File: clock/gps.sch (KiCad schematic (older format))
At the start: 16 parts, among them P301 MCRF, Q301 BSS138, Q302 BSS138, U301 Adafruit746, U302 MIC5225, U303 PA6H

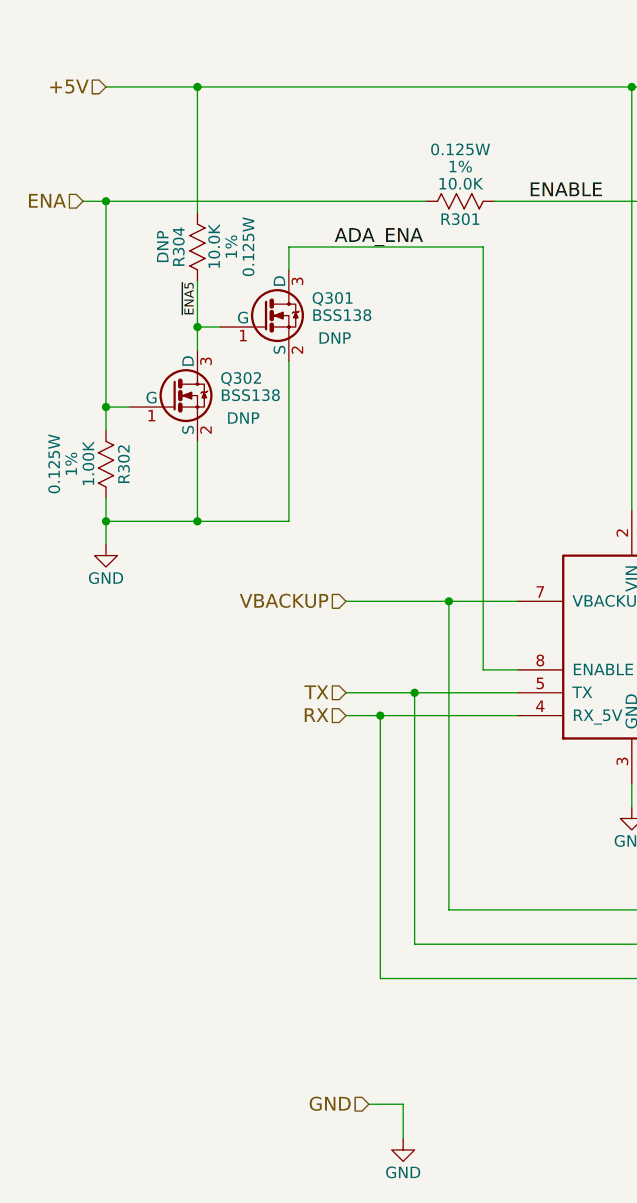
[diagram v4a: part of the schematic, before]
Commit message: Remove sheet to sheet power interconnect because power symbols are global.
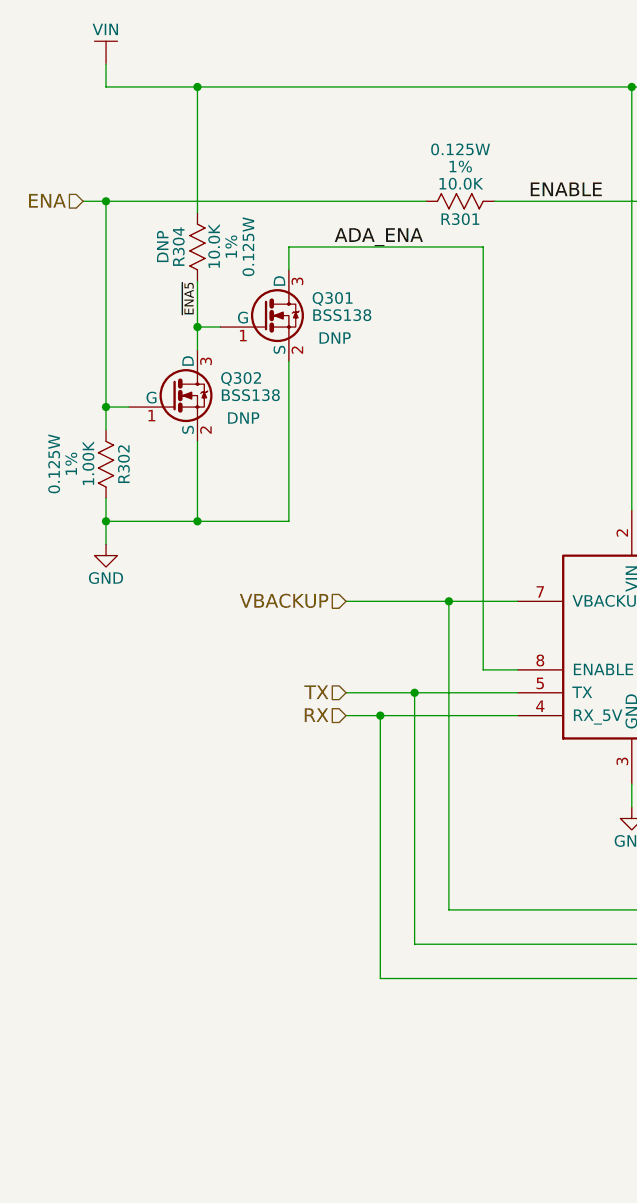
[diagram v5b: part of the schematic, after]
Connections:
- net +5V renamed VIN
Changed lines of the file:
@@
 $EndComp
 $Comp
-L GND #PWR305
+L GND #PWR042
 U 1 1 56235A8F
 P 7200 5350
-F 0 "#PWR305" H 7200 5100 50  0001 C CNN
+F 0 "#PWR042" H 7200 5100 50  0001 C CNN
 F 1 "GND" H 7200 5200 50  0000 C CNN
 F 2 "" H 7200 5350 60  0000 C CNN
@@
 Connection ~ 7100 1900
 $Comp
-L GND #PWR306
+L GND #PWR043
 U 1 1 56235D57
 P 8000 2650
-F 0 "#PWR306" H 8000 2400 50  0001 C CNN
+F 0 "#PWR043" H 8000 2400 50  0001 C CNN
 F 1 "GND" H 8000 2500 50  0000 C CNN
 F 2 "" H 8000 2650 60  0000 C CNN
@@
 Connection ~ 5250 2550
 Connection ~ 7100 2550
-Text HLabel 1450 1600 0    60   Input ~ 0
-+5V
 Text HLabel 1350 2100 0    60   Input ~ 0
 ENA
@@
 	5200 3650 6300 3650
 $Comp
-L GND #PWR304
+L GND #PWR044
 U 1 1 56236310
 P 4950 3350
-F 0 "#PWR304" H 4950 3100 50  0001 C CNN
+F 0 "#PWR044" H 4950 3100 50  0001 C CNN
 F 1 "GND" H 4950 3200 50  0000 C CNN
 F 2 "" H 4950 3350 60  0000 C CNN
@@
 	2500 3850 3250 3850
 $Comp
-L GND #PWR303
+L GND #PWR045
 U 1 1 56236487
 P 3750 4750
-F 0 "#PWR303" H 3750 4500 50  0001 C CNN
+F 0 "#PWR045" H 3750 4500 50  0001 C CNN
 F 1 "GND" H 3750 4600 50  0000 C CNN
 F 2 "" H 3750 4750 60  0000 C CNN
@@
 Wire Wire Line
 	7100 2300 7100 2550
-Text HLabel 2600 6050 0    60   Input ~ 0
-GND
-$Comp
-L GND #PWR302
-U 1 1 5624967B
-P 2750 6200
-F 0 "#PWR302" H 2750 5950 50  0001 C CNN
-F 1 "GND" H 2750 6050 50  0000 C CNN
-F 2 "" H 2750 6200 60  0000 C CNN
-F 3 "" H 2750 6200 60  0000 C CNN
-	1    2750 6200
-	1    0    0    -1
-$EndComp
-Wire Wire Line
-	2750 6200 2750 6050
-Wire Wire Line
-	2750 6050 2600 6050
 $Comp
 L C C302
@@
 FILT_GPS_3.3V
 $Comp
-L PWR_FLAG #FLG301
+L PWR_FLAG #FLG046
 U 1 1 5643829E
 P 7750 1800
-F 0 "#FLG301" H 7750 1895 50  0001 C CNN
+F 0 "#FLG046" H 7750 1895 50  0001 C CNN
 F 1 "PWR_FLAG" H 7750 1980 50  0000 C CNN
 F 2 "" H 7750 1800 60  0000 C CNN
@@
 Connection ~ 4050 1900
 $Comp
-L GND #PWR301
+L GND #PWR047
 U 1 1 57AB6F8A
 P 1450 3600
-F 0 "#PWR301" H 1450 3350 50  0001 C CNN
+F 0 "#PWR047" H 1450 3350 50  0001 C CNN
 F 1 "GND" H 1450 3450 50  0000 C CNN
 F 2 "" H 1450 3600 60  0000 C CNN
@@
 	8700 2300 8700 2400
 $Comp
-L GND #PWR307
+L GND #PWR048
 U 1 1 5897F426
 P 8700 2900
-F 0 "#PWR307" H 8700 2650 50  0001 C CNN
+F 0 "#PWR048" H 8700 2650 50  0001 C CNN
 F 1 "GND" H 8700 2750 50  0000 C CNN
 F 2 "" H 8700 2900 60  0000 C CNN
@@
 	8700 1900 8700 2000
 Connection ~ 8000 1900
+$Comp
+L VIN #PWR049
+U 1 1 589872B7
+P 1450 1500
+F 0 "#PWR049" H 1450 1350 50  0001 C CNN
+F 1 "VIN" H 1450 1650 50  0000 C CNN
+F 2 "" H 1450 1500 60  0000 C CNN
+F 3 "" H 1450 1500 60  0000 C CNN
+	1    1450 1500
+	1    0    0    -1
+$EndComp
+Wire Wire Line
+	1450 1600 1450 1500
 $EndSCHEMATC

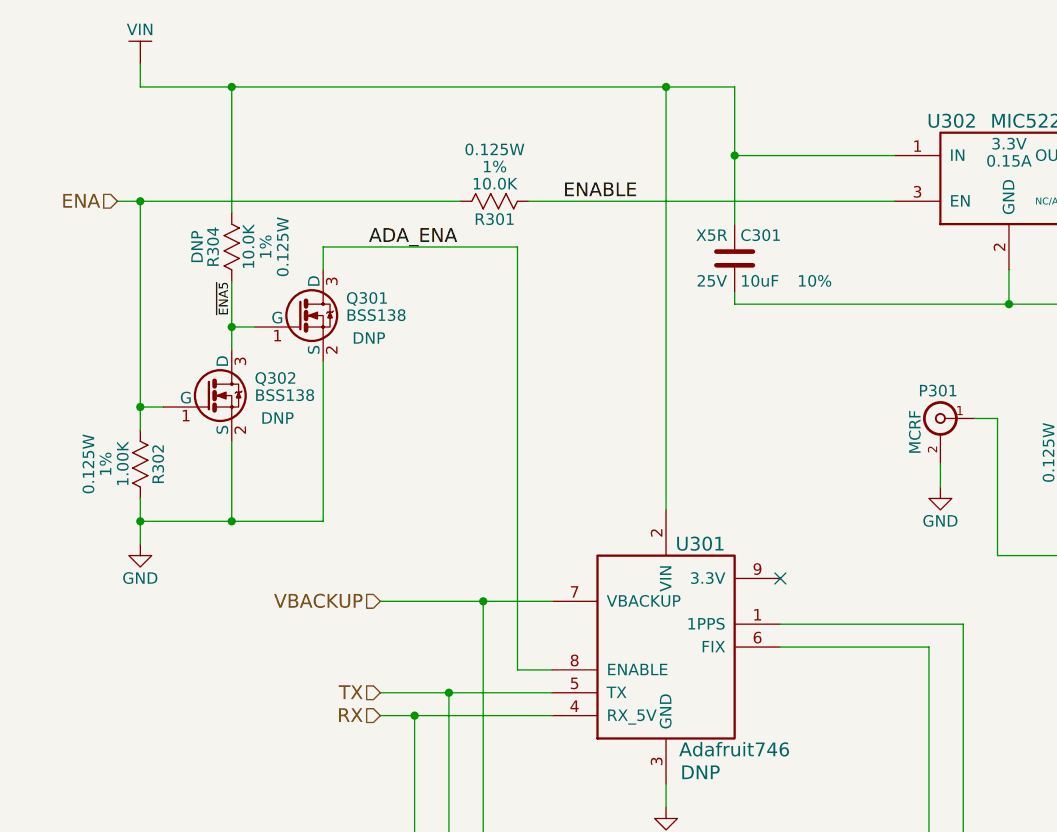
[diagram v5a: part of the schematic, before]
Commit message: Move power indicator LEDs. Clean up test points and silkscreen. Move the gate of Q302 to the other side of R301.
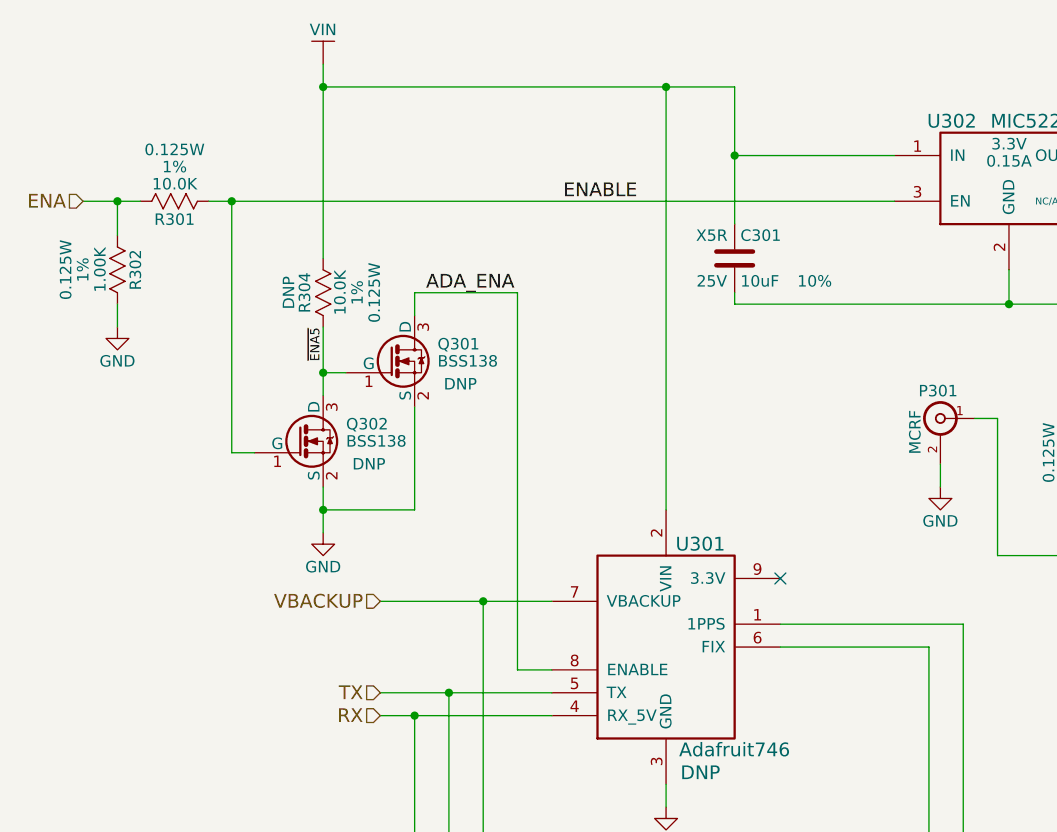
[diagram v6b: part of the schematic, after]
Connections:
- net ENA: no longer Q302.1 (G)
- net ENABLE: now also Q302.1 (G)
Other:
- moved on the sheet: Q301, Q302, R301, R302, R304

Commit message: Separate RTC interrupt to allow for different IO register clock domain.
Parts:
- R302: PartNum CRCW080510K0FKEA -> CRCW08051K00FKEA
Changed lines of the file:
@@
 F 5 "0.125W" V 1125 2400 50  0000 C CNN "Power"
 F 6 "Vishay Dale" V 1350 2400 50  0001 C CNN "Manufacturer"
-F 7 "CRCW080510K0FKEA" V 1500 2400 50  0001 C CNN "PartNum"
+F 7 "CRCW08051K00FKEA" V 1500 2400 50  0001 C CNN "PartNum"
 	1    1350 2400
 	1    0    0    -1
